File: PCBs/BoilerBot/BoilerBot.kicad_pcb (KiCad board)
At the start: 2 copper layers, 100 x 34 mm, 24 parts, among them J1 Screw_Terminal_01x02, J10 Conn_01x03_Male, J2 Screw_Terminal_01x03, J3 Screw_Terminal_01x03, J4 Screw_Terminal_01x02, J5 Conn_01x05_Male, J6 Conn_01x03_Male, J7 Conn_01x03_Male, J8 Screw_Terminal_01x03, J9 Conn_01x04_Male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

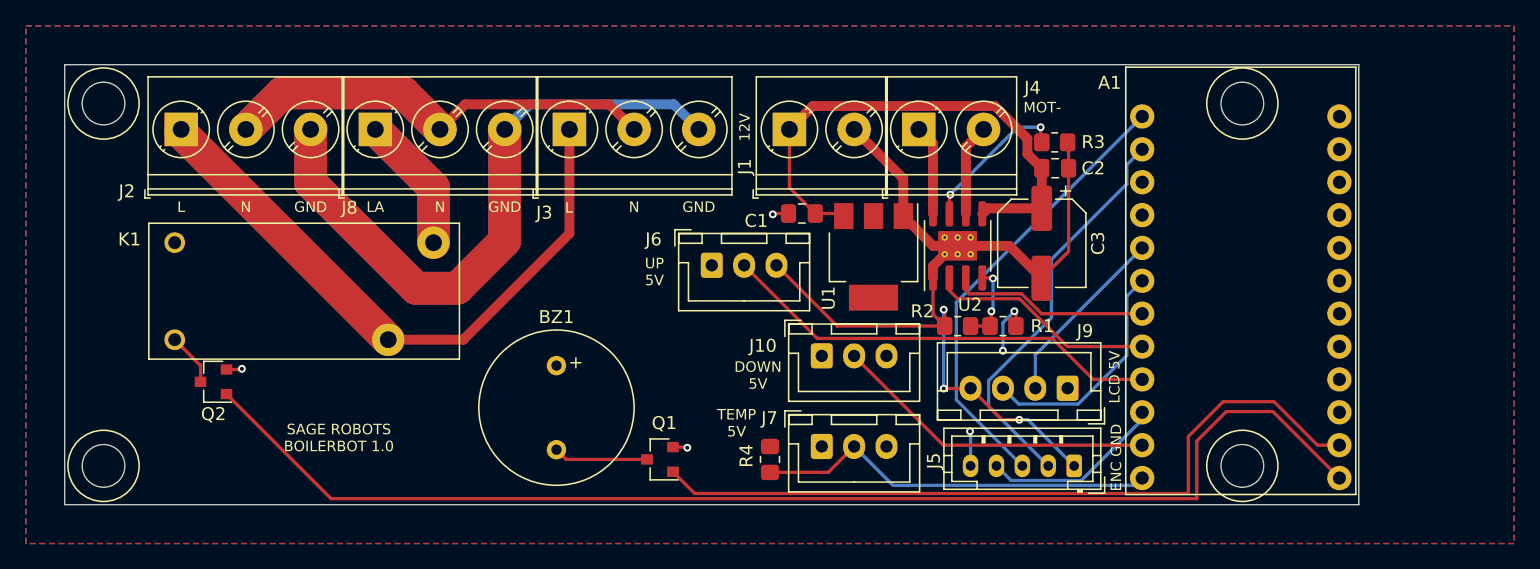
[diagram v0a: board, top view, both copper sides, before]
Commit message: updates for off board PDB
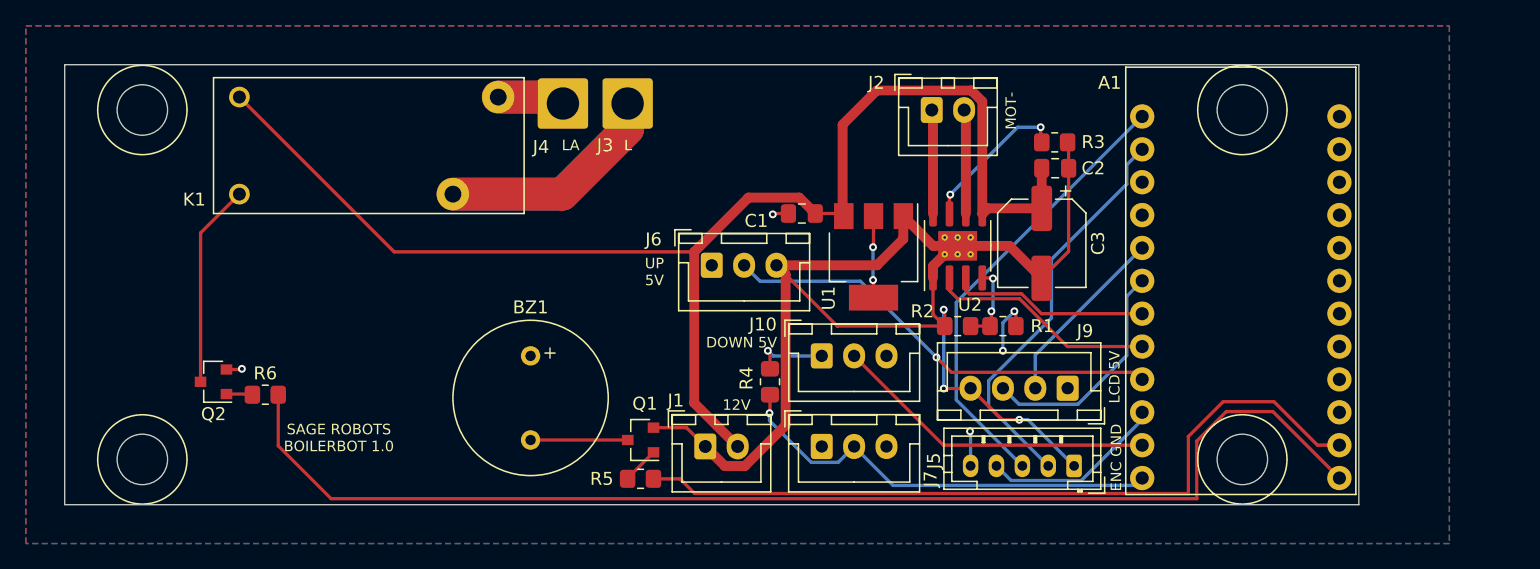
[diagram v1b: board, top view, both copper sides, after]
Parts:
- removed J8: Screw_Terminal_01x03, TerminalBlock_Phoenix:TerminalBlock_Phoenix_PT-1,5-3-5.0-H_1x03_P5.00mm_Horizontal
- added R5: 100, Resistor_SMD:R_0805_2012Metric_Pad1.20x1.40mm_HandSolder, F.Cu at (122.5, 80.0)
- added R6: 100, Resistor_SMD:R_0805_2012Metric_Pad1.20x1.40mm_HandSolder, F.Cu at (93.5, 73.5)
- J1: value Screw_Terminal_01x02 -> Conn_01x02_Male; footprint TerminalBlock_Phoenix:TerminalBlock_Phoenix_PT-1,5-2-5.0-H_1x02_P5.00mm_Horizontal -> Connector_JST:JST_XH_B2B-XH-A_1x02_P2.50mm_Vertical
- J2: value Screw_Terminal_01x03 -> Conn_01x02_Male; footprint TerminalBlock_Phoenix:TerminalBlock_Phoenix_PT-1,5-3-5.0-H_1x03_P5.00mm_Horizontal -> Connector_JST:JST_XH_B2B-XH-A_1x02_P2.50mm_Vertical
- J3: value Screw_Terminal_01x03 -> Conn_01x01_Male; footprint TerminalBlock_Phoenix:TerminalBlock_Phoenix_PT-1,5-3-5.0-H_1x03_P5.00mm_Horizontal -> Connector_Wire:SolderWire-2sqmm_1x01_D2mm_OD3.9mm
- J4: value Screw_Terminal_01x02 -> Conn_01x01_Male; footprint TerminalBlock_Phoenix:TerminalBlock_Phoenix_PT-1,5-2-5.0-H_1x02_P5.00mm_Horizontal -> Connector_Wire:SolderWire-2sqmm_1x01_D2mm_OD3.9mm
- R1: value 3.3K -> 10k
- moved J2 58.0 mm to (145.0, 51.5)
- moved J4 27.6 mm to (116.5, 51.0)
- moved J1 25.3 mm to (127.5, 77.5)
- moved K1 12.3 mm to (101.5, 54.2)
- moved R4 6.00 mm to (132.5, 72.5)
- moved J3 4.92 mm to (121.5, 51.0)
- moved BZ1 2.14 mm to (114.0, 73.8)
- moved Q1 2.12 mm to (122.5, 77.0)
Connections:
- J1 pad 1: +12V -> GND
- J1 pad 2: GND -> +12V
- J2 pad 1: L -> Net-(J2-Pad1)
- J2 pad 2: N -> Net-(J2-Pad2)
- J4 pad 1: Net-(J4-Pad1) -> LA
- K1 pad 1: +5V -> +12V
- Q1 pad 1: BUZZ -> Net-(Q1-Pad1)
- Q2 pad 1: HEAT -> Net-(Q2-Pad1)
- U2 pad 6: Net-(J4-Pad2) -> Net-(J2-Pad2)
- U2 pad 8: Net-(J4-Pad1) -> Net-(J2-Pad1)
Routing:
- net +12V: track 40.4 -> 106.3 mm
- net GND: track 159.0 -> 105.5 mm, vias 6 -> 5
- net N: track 51.3 -> 0.00 mm
- net L: track 71.2 -> 35.1 mm
- net +5V: track 7.30 -> 19.4 mm, vias 3 -> 6
- net Net-(K1-Pad6): track 4.08 -> 15.7 mm
- net LA: track 21.2 -> 10.4 mm
- net Net-(J2-Pad2): track 0.00 -> 8.08 mm
- net Net-(J2-Pad1): track 0.00 -> 8.06 mm
- net Net-(J4-Pad2): track 7.09 -> 0.00 mm
- net Net-(J4-Pad1): track 6.98 -> 0.00 mm
- net TEMP: track 31.1 -> 34.1 mm, vias 0 -> 1
- net Net-(Q1-Pad1): track 0.00 -> 2.88 mm
- net Net-(Q2-Pad1): track 0.00 -> 2.02 mm
- net HEAT: track 96.9 -> 95.2 mm
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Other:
- outline, holes or cut-outs redrawn
- board text removed: "GND"
- board text removed: "N"
- board text removed: "TEMP 5V"
